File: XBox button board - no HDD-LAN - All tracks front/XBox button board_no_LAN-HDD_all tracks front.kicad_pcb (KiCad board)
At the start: 2 copper layers, 80 x 40.6 mm, 9 parts, among them J1 Conn_01x09_Pin

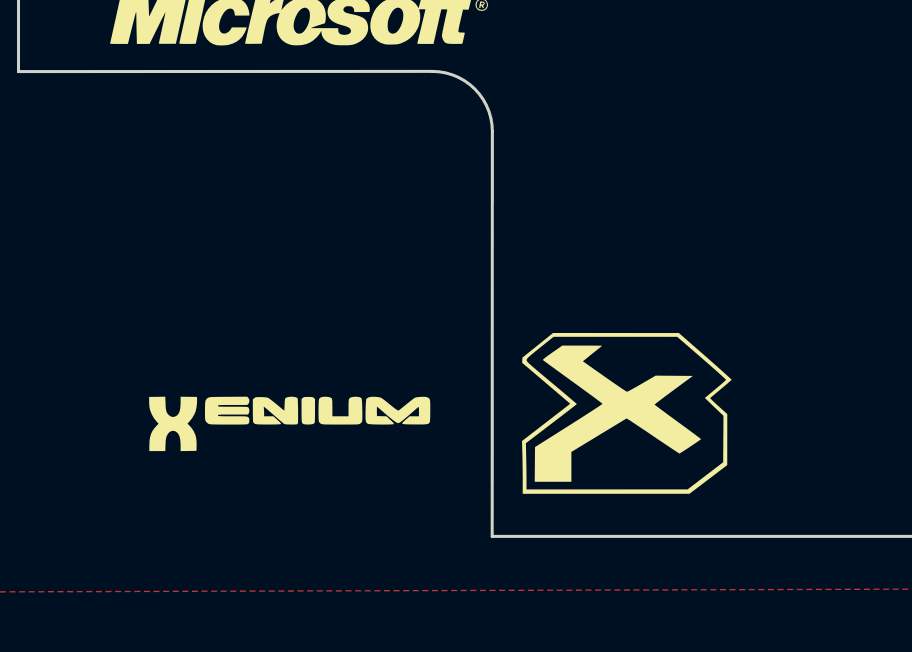
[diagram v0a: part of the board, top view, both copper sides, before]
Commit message: Minor image adjustment
moved some graphics
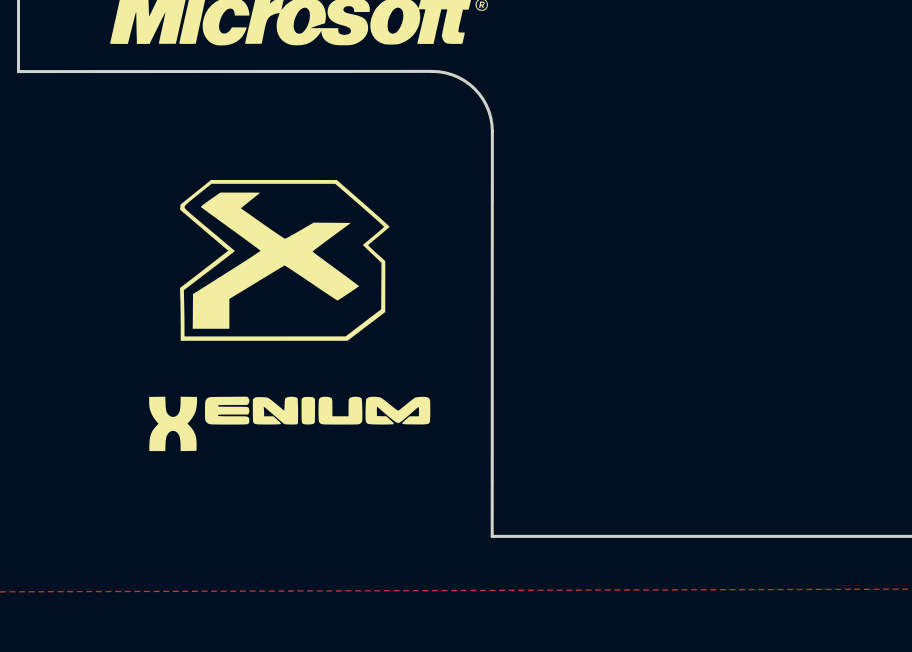
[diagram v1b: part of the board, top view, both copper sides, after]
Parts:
- moved G*** 12.5 mm to (118.2, 109.4)

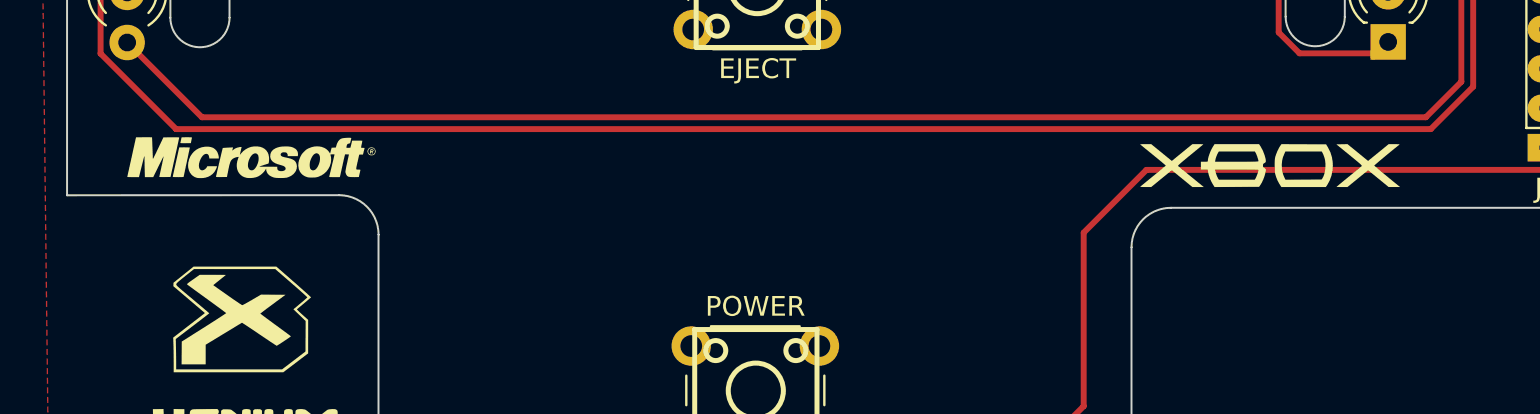
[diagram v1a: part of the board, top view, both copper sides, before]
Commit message: updated silkscreens
removed logos from silk print area
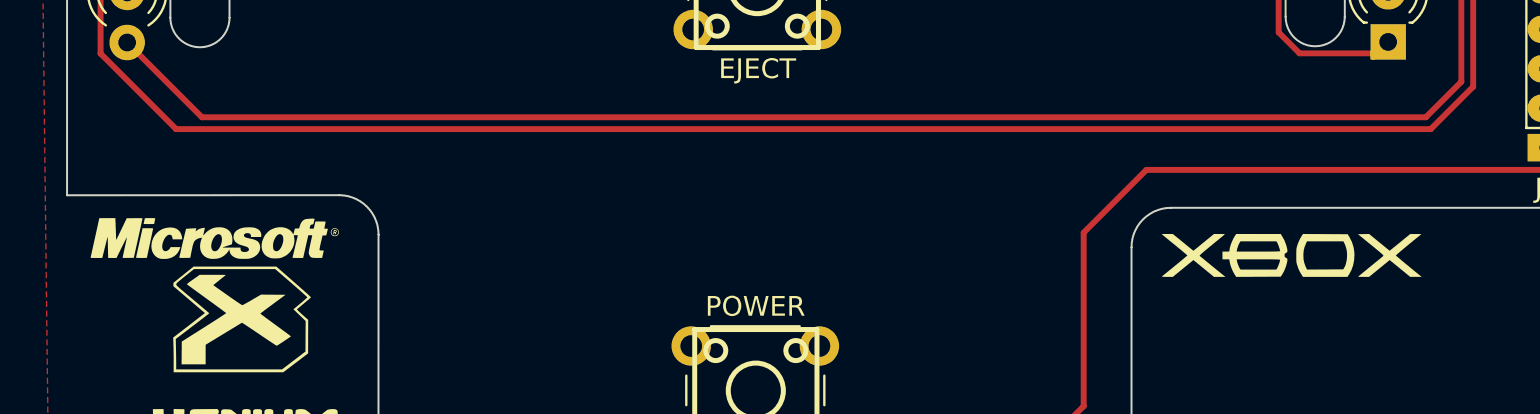
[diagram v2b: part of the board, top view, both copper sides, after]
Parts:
- moved G*** 4.69 mm to (171.3, 106.2)
- moved G*** 4.50 mm to (116.8, 105.3)
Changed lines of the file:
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@@
 	(footprint "LOGO"
 		(layer "F.Cu")
-		(at 170.254788 101.693806)
+		(at 171.35 106.25)
 		(property "Reference" "G***"
 			(at 0 0 0)
@@
 	(footprint "LOGO"
 		(layer "F.Cu")
-		(at 118.61083 101.2)
+		(at 116.75 105.3)
 		(property "Reference" "G***"
 			(at 0 0 0)
